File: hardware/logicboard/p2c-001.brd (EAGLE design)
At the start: 91 x 55 mm, 50 parts, among them IC1 74LS07N, J1 POWER_JACKSLT, J2 RLY, J3 I2C, J4 DISP, J5 DIN5, J6 DIN5, K1 G5V1, Q1 220mA/50V/3.5Ω, Q2 220mA/50V/3.5Ω, SW1 A6A-16R, T1 2SC1815, U1 DS18B20

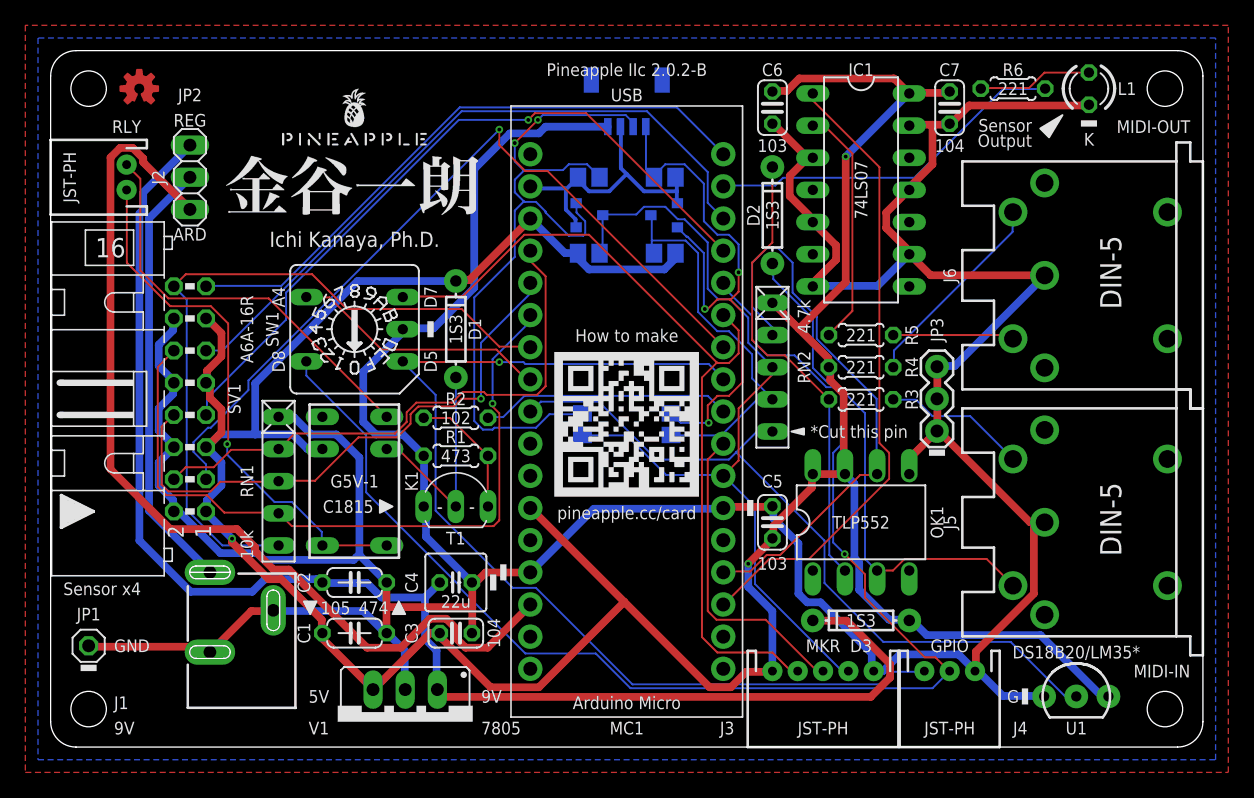
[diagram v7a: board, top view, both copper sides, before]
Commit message: Modified schematic for better readability.
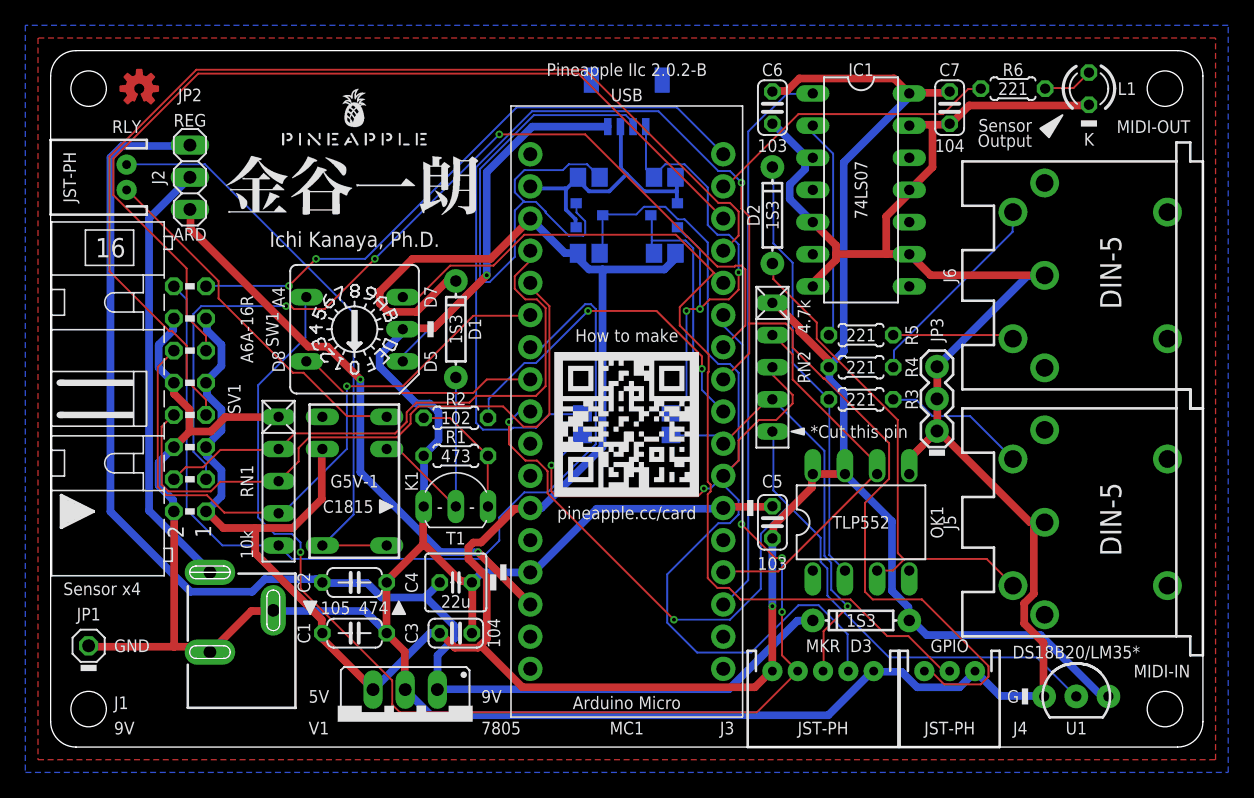
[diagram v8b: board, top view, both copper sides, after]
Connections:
- net DISP1 renamed GPIO1
- net IN+ renamed MISEND
- net IN- renamed MIRETN
- net OUT+ renamed MOSEND
- net OUT- renamed MORETN
- net SCL3V3 renamed SCL3V
- net SDA3V3 renamed SDA3V
- removed net +9V: JP2.3, U$2.P$20
- removed net DISP2: J4.2, SW1.8, U$2.P$5
- removed net LED0: U$2.P$34
- removed net N$4: J2.2, K1.10
- removed net N$6: J2.1, K1.5, K1.6
- new net 9V: J1.PWR, JP2.2
- new net GPIO2: J4.2, SW1.4, U$2.P$5
- new net RLYA: J2.1, K1.10
- new net RLYB: J2.2, K1.5, K1.6
- net A4: now also SW1.8; no longer SW1.2
- net D7: now also SW1.2; no longer SW1.4
- net LED1: now also R6.2; no longer R6.1
- net N$1: now also R6.1; no longer R6.2
- net VIN: now also JP2.3, U$2.P$20; no longer J1.PWR, JP2.2
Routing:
- net DISP2: track 106.1 -> 0.00 mm, vias 1 -> 0
- net GPIO2: track 0.00 -> 77.5 mm
- net +9V: track 76.4 -> 0.00 mm
- net RLYB: track 0.00 -> 47.3 mm
- net N$6: track 42.3 -> 0.00 mm, vias 1 -> 0
- net D7: track 67.5 -> 103.5 mm, vias 0 -> 4
- net 9V: track 0.00 -> 34.5 mm
- net SDA: track 67.8 -> 101.5 mm, vias 0 -> 2
- net N$4: track 33.1 -> 0.00 mm
- net RLYA: track 0.00 -> 28.8 mm
- net DTCT2: track 57.2 -> 84.5 mm, vias 1 -> 0
- net GPIO1: track 83.5 -> 106.6 mm
- net DTCT3: track 53.6 -> 73.9 mm
- net THS: track 59.1 -> 76.7 mm, vias 0 -> 2
- net ANLG4: track 57.4 -> 74.2 mm
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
